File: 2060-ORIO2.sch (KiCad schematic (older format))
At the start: 195 parts, among them J11 RaspberryPI-B+header, J12 Conn_01x04, J13 Conn_01x08, J14 Conn_01x02, J15 Conn_01x08, J16 Conn_01x10, J17 Conn_01x10, J18 Conn_01x10, J19 Conn_01x10, J20 Conn_01x09, J21 Conn_01x08, J22 Conn_01x08, J23 Conn_01x08, J24 Conn_01x08, J25 Conn_01x08, J26 Conn_01x08, J27 Conn_01x02, J28 Conn_01x16, J29 Conn_01x16, J30 Conn_01x16, J31 Conn_01x08, J32 Conn_01x08, J33 Conn_01x08, J34 Conn_01x08, J35 TBL001-500-02GY-2GY, Q11 ULN2803ADWR, Q12 BCV27, SW11 SW_DIP_x08, U11 ICE40HX4K-TQ144, U12 SN74LVC4245AN, U13 SN74LVC4245AN, U14 SN74LVC4245AN, U15 TPS563231, U16 MCP3008, U17 AZ1117CH-3.3TRG1, U18 AZ1117CH-3.3TRG1, U19 AZ1117CH-1.2, U20 TPS563231, U21 SN74LVC4245AN, U22 SN74LVC4245AN, U23 SN74LVC4245AN, U24 SN74LVC4245AN, U25 TPS563231, U26 AP3012, Y11 XLH536025_000000I

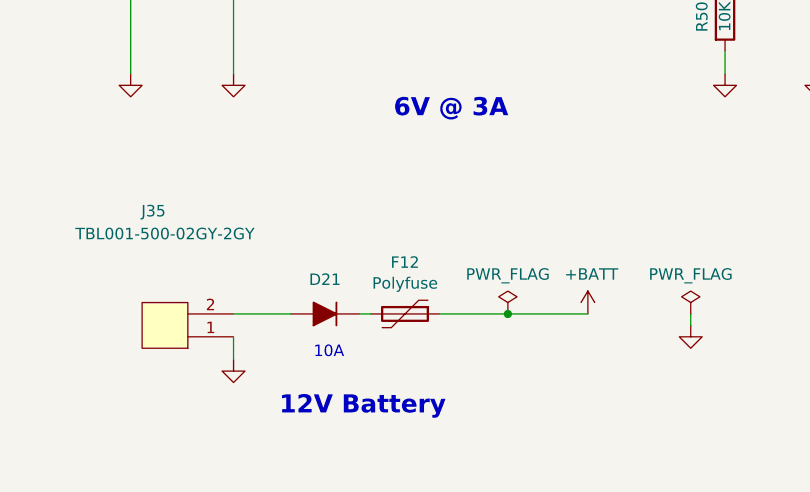
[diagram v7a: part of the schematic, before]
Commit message: Final BOM review & corrections to values.
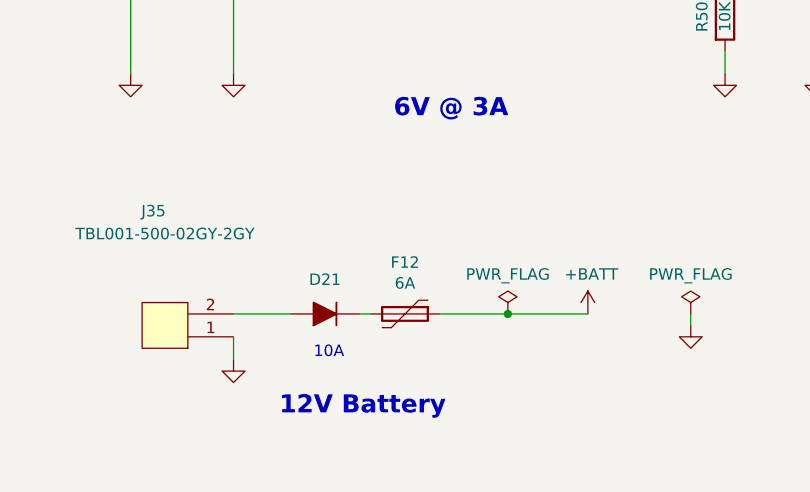
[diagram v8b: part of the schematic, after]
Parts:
- F12: value Polyfuse -> 6A; Description (none) -> PTC RESET FUSE 12V 6A 2920; Digi-Key_PN (none) -> F8137CT-ND; MPN (none) -> 2920L600/12MR; Manufacturer (none) -> Littelfuse Inc.
- J12: Digi-Key_PN 2057-PH1-04-UA-ND -> (none)
- J13, J14, J15, J20, J21, J22, J23, J24, J25, J26, J27, J28, J29, J30, J31, J32, J33, J34, LOGO11, NT1: Description (none) -> x; Digi-Key_PN (none) -> x; MPN (none) -> x; Manufacturer (none) -> x
- R23, R24, R27: Description (none) -> RES SMD 2.2K OHM 1% 1/10W 0603; MPN (none) -> RC0603FR-072K2L; Manufacturer (none) -> Yageo
- R25: Description (none) -> RES SMD 33K OHM 1% 1/10W 0603; MPN (none) -> RC0603FR-0733KL; Manufacturer (none) -> Yageo
- R26: Description (none) -> RES SMD 3.3K OHM 1% 1/10W 0603; MPN (none) -> RC0603FR-073K3L; Manufacturer (none) -> Yageo
- R52: Description RES SMD 4.7K OHM 1% 1/10W 0603 -> RES SMD 5.1K OHM 1% 1/10W 0603; Digi-Key_PN 311-4.70KHRCT-ND -> CR0603-FX-5101ELFCT-ND; MPN RC0603FR-074K7L -> CR0603-FX-5101ELF; Manufacturer Yageo -> Bourns Inc.
- R53: Description (none) -> RES SMD 1K OHM 1% 1/10W 0603; Digi-Key_PN (none) -> 311-1.00KHRCT-ND; MPN (none) -> RC0603FR-071KL
- R54: Description (none) -> RES SMD 1K OHM 1% 1/10W 0603; Digi-Key_PN (none) -> 311-1.00KHRCT-ND; MPN (none) -> RC0603FR-071KL; Manufacturer (none) -> Yageo
- RN1, RN2, RN3, RN4: Description RES ARRAY 8 RES 330 OHM 1506 -> RES ARRAY 8 RES 10K OHM 1506; Digi-Key_PN Y1331CT-ND -> Y1103CT-ND; MPN EXB-2HV331JV -> EXB-2HV103JV
- U15, U20, U25: Manufacturer (none) -> Texas Instruments
